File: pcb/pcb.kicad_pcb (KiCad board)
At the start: 2 copper layers, 70 x 21 mm, 20 parts, among them J1 BAT+, J2 BAT-, J3 Molex, SW1 Reset, SW2 Flash, U1 BOB-13263, U2 ESP-12F, U3 TP4056, U4 GY-521, U5 VREG

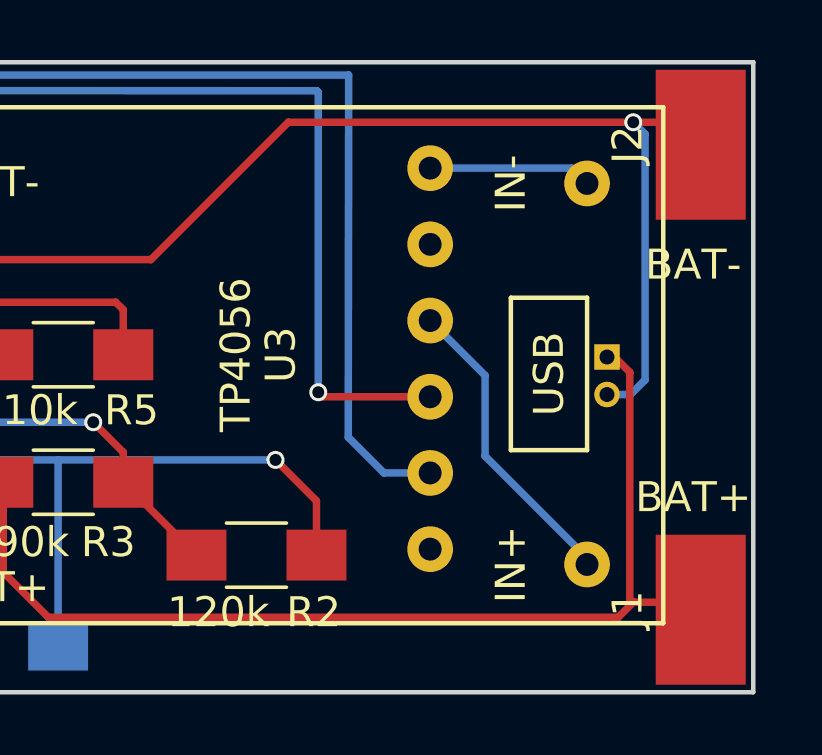
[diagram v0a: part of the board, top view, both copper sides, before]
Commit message: PCB: use a smaller FTDI breakout board
The CP2102 USB Micro breakout boards look like they fit between the
pins of the TP4056 breakout board, which simplifies installation.
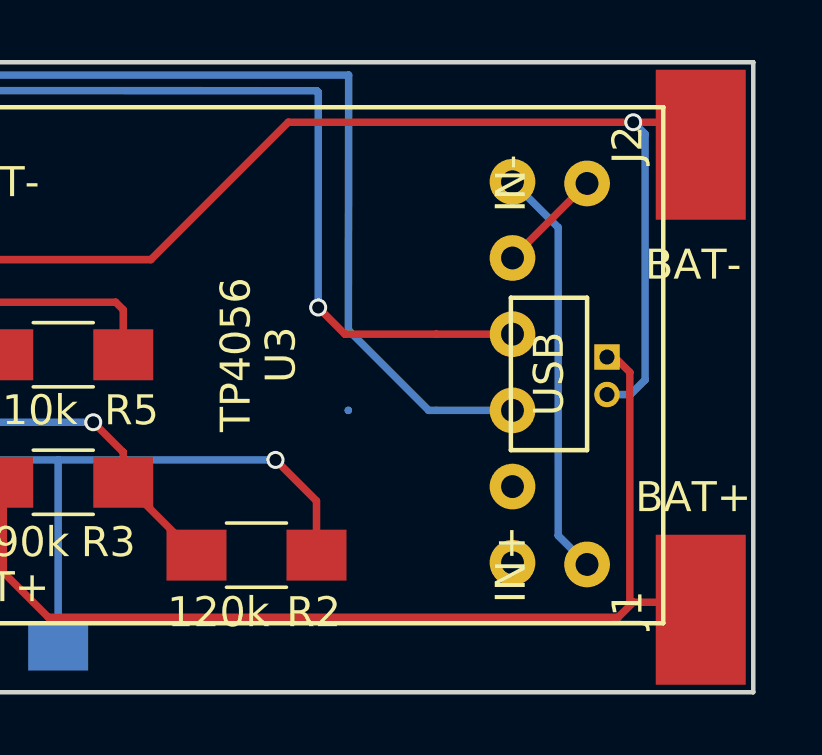
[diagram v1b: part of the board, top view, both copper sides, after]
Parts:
- U1: value BOB-13263 -> CP2102; footprint BOB13263:BOB-13263-TOP -> CP2102-BRK:CP2102-BREAKOUT
- moved U1 17.6 mm to (153.2, 105.7), turned to 0 degrees
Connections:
- U1 pad 2: /HostRX -> (no net)
- U1 pad 3: /HostTX -> /HostRX
- U1 pad 4: /USB+ -> /HostTX
- U1 pad 5: (no net) -> /USB-
- U1 pad 6: /USB- -> /USB+
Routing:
- net /USB+: track 10.3 -> 13.8 mm
- net /USB-: track 5.44 -> 3.51 mm

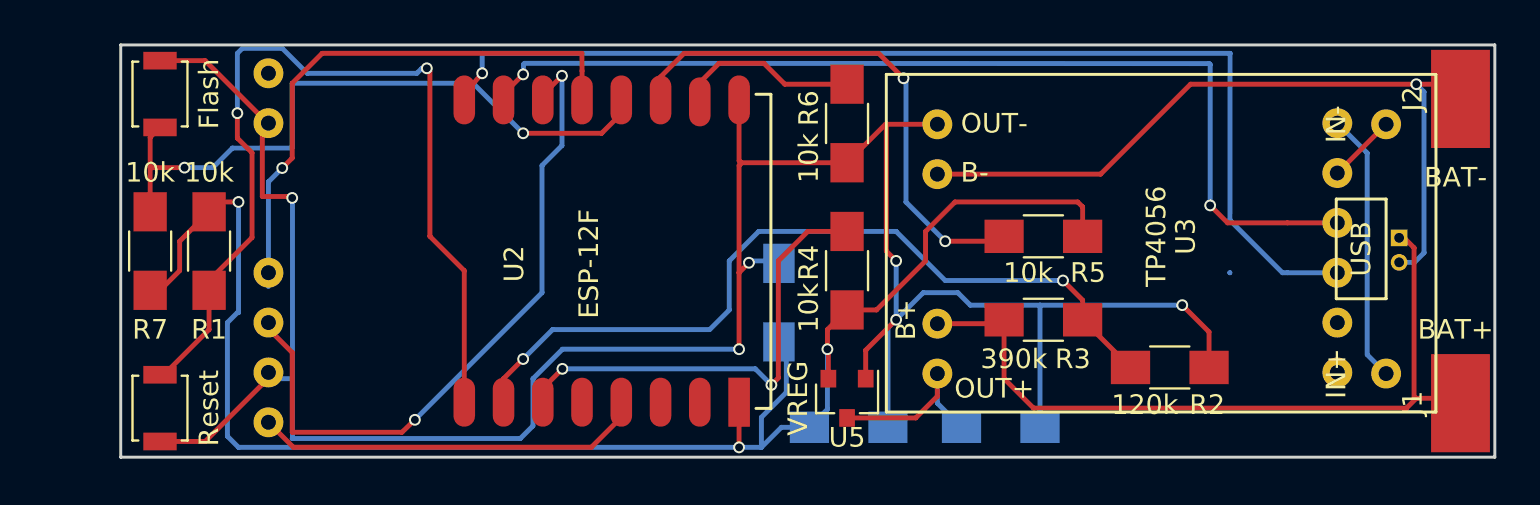
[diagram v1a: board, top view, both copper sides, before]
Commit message: Some more minor touch-ups
1. Remove silkscreen from pads which will take soldering
2. Fix some trace-via clearance issues (min 5 mil)
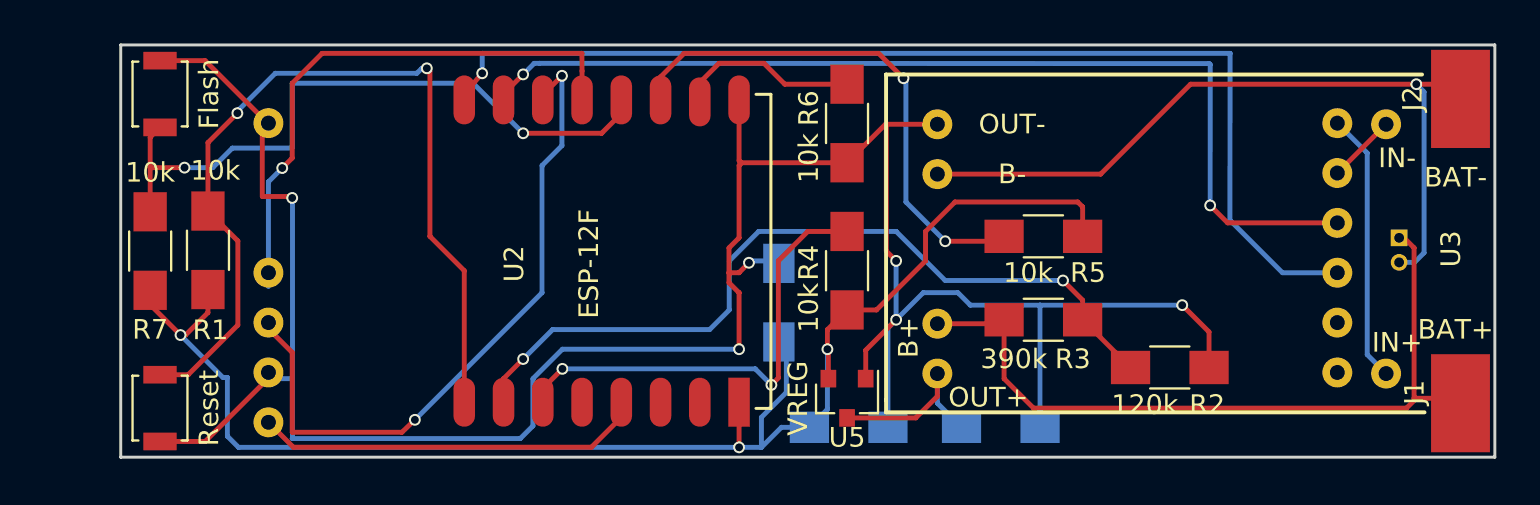
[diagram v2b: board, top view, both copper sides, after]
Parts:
- moved R1 0.07 mm to (114.7, 98.2), turned to 90 degrees
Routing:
- net /3.3+: track 84.7 -> 77.7 mm
- net Net-(R1-Pad2): track 46.2 -> 45.0 mm
- net /GND: track 129.2 -> 130.1 mm

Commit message: More trace cleanup:
1. Remove right angles
2. Thicker USB+/-, charger +/-, 3.3, GND traces
3. Improve 3.3 and GND routing: more like rails and traces to
components, less daisy-chaining
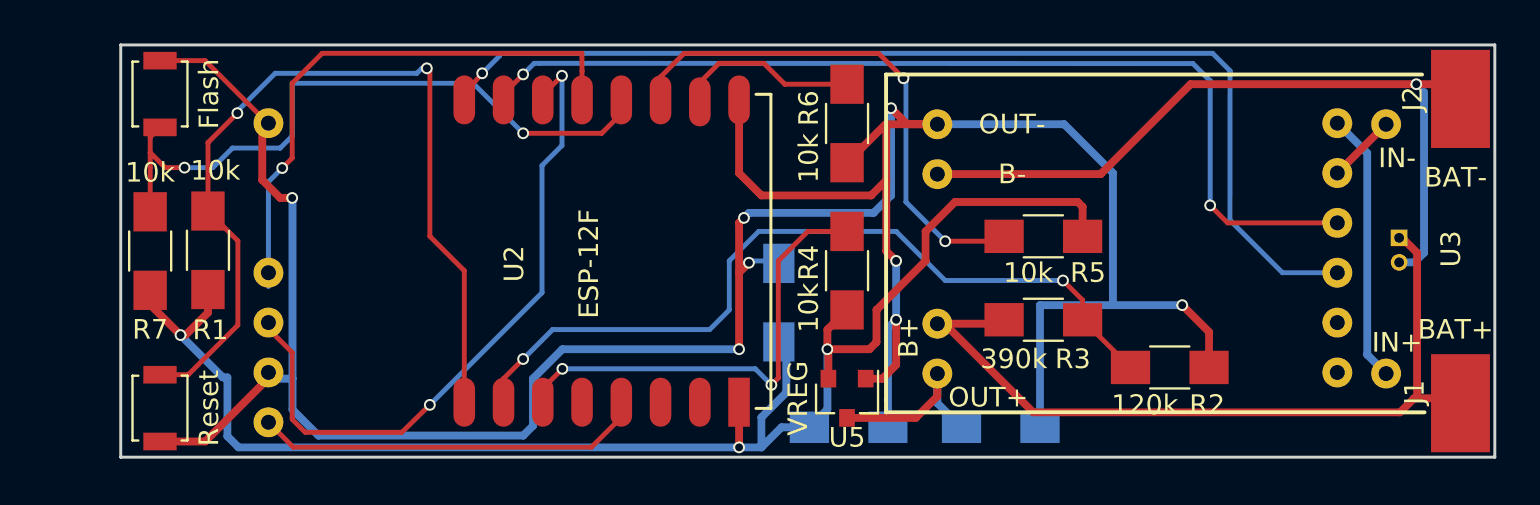
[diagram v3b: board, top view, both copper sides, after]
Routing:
- net /GND: track 130.1 -> 152.5 mm, vias 6 -> 8
- net /3.3+: track 77.7 -> 80.5 mm
- net /BAT+: track 39.6 -> 41.0 mm
- net /HostRX: track 56.6 -> 55.5 mm

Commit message: GY521 dimensions update (to match measured size on my workbench)
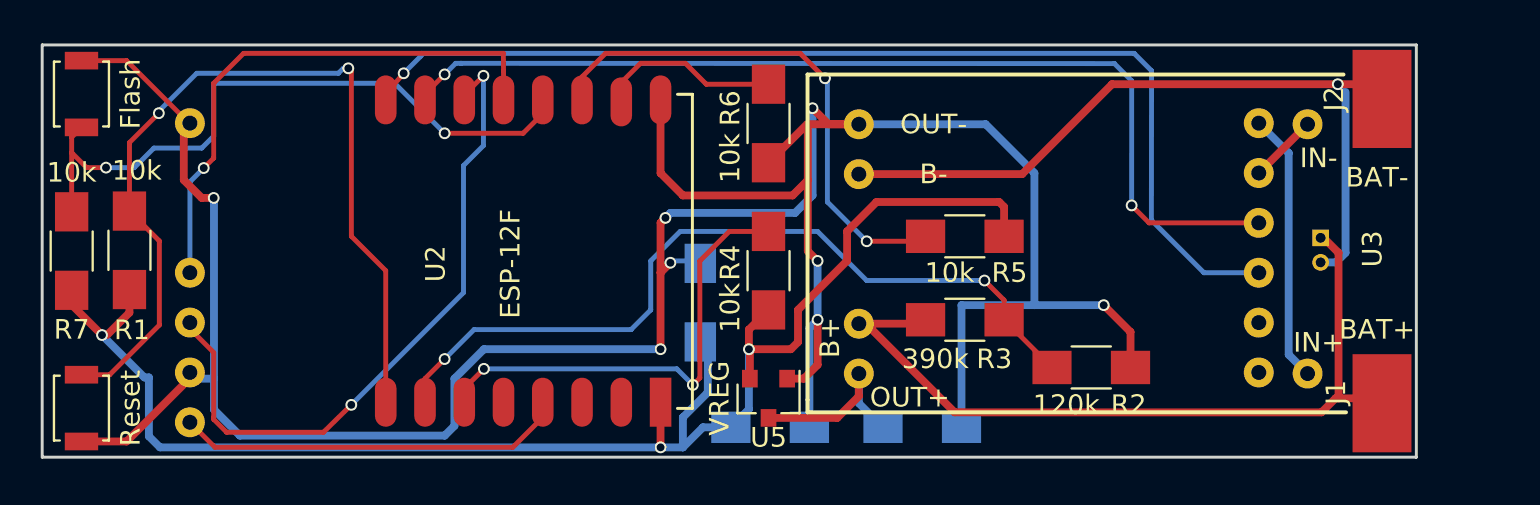
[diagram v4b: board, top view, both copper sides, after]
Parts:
- moved C1 4.00 mm to (139.8, 100.8)
- moved C2 4.00 mm to (151.1, 107.2)
- moved C3 4.00 mm to (143.3, 107.2)
- moved J1 4.00 mm to (174.5, 106.0)
- moved J2 4.00 mm to (174.5, 90.5)
- moved J3 4.00 mm to (171.4, 97.5)
- moved R1 4.00 mm to (110.7, 98.2)
- moved R2 4.00 mm to (159.7, 104.1)
- moved R3 4.00 mm to (153.2, 101.7)
- moved R4 4.00 mm to (143.2, 99.2)
- moved R5 4.00 mm to (153.2, 97.5)
- moved R6 4.00 mm to (143.2, 91.7)
- moved R7 4.00 mm to (107.7, 98.2)
- moved SW1 4.00 mm to (108.2, 106.2)
- moved SW2 4.00 mm to (108.2, 90.2)
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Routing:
- net /SDA: track 29.3 -> 28.6 mm

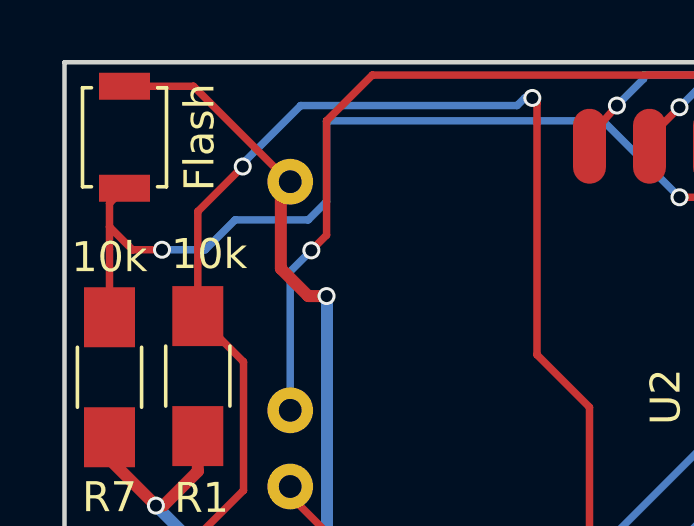
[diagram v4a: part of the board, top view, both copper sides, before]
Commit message: Move board in page (ugh)
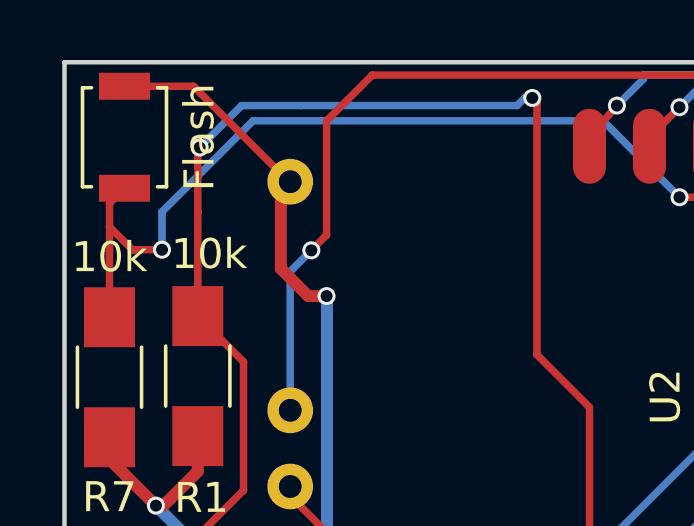
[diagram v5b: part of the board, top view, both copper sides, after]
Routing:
- net Net-(R1-Pad2): track 45.0 -> 46.2 mm
- net Net-(R7-Pad2): track 33.7 -> 32.8 mm
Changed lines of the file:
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@@
     (links 41)
     (no_connects 0)
-    (area 99.037601 87.234999 180.536601 118.560001)
+    (area 106.162599 87.634999 176.312601 108.785001)
     (thickness 1.6)
     (drawings 17)
@@
   (segment (start 151.2376 101.71) (end 151.0376 101.91) (width 0.25) (layer F.Cu) (net 5) (status 30))
   (segment (start 151.0376 101.91) (end 147.8376 101.91) (width 0.4) (layer F.Cu) (net 5) (status 30))
-  (segment (start 110.681 96.171) (end 110.681 92.6846) (width 0.25) (layer F.Cu) (net 6) (status 10))
-  (segment (start 112.1796 91.186) (end 112.1796 91.0844) (width 0.25) (layer B.Cu) (net 6))
+  (segment (start 110.681 92.71) (end 110.681 90.614) (width 0.25) (layer F.Cu) (net 6))
+  (segment (start 123.7376 99.21) (end 121.9876 97.46) (width 0.25) (layer F.Cu) (net 6))
+  (segment (start 121.9876 89.056) (end 121.9876 97.46) (width 0.25) (layer F.Cu) (net 6))
+  (segment (start 121.8316 88.9) (end 121.9876 89.056) (width 0.25) (layer F.Cu) (net 6))
+  (segment (start 123.7376 99.21) (end 123.7376 105.21) (width 0.25) (layer F.Cu) (net 6) (status 20))
+  (via (at 121.8316 88.9) (size 0.6) (drill 0.4) (layers F.Cu B.Cu) (net 6))
+  (segment (start 121.5776 88.9) (end 121.8316 88.9) (width 0.25) (layer B.Cu) (net 6))
+  (segment (start 121.3236 89.154) (end 121.5776 88.9) (width 0.25) (layer B.Cu) (net 6))
   (segment (start 114.11 89.154) (end 121.3236 89.154) (width 0.25) (layer B.Cu) (net 6))
-  (segment (start 112.1796 91.0844) (end 114.11 89.154) (width 0.25) (layer B.Cu) (net 6))
-  (segment (start 121.3236 89.154) (end 121.5776 88.9) (width 0.25) (layer B.Cu) (net 6))
-  (segment (start 121.5776 88.9) (end 121.8316 88.9) (width 0.25) (layer B.Cu) (net 6))
-  (via (at 121.8316 88.9) (size 0.6) (drill 0.4) (layers F.Cu B.Cu) (net 6))
-  (via (at 112.1796 91.186) (size 0.6) (drill 0.4) (layers F.Cu B.Cu) (net 6))
-  (segment (start 123.7376 99.21) (end 123.7376 105.21) (width 0.25) (layer F.Cu) (net 6) (status 20))
-  (segment (start 121.8316 88.9) (end 121.9876 89.056) (width 0.25) (layer F.Cu) (net 6))
-  (segment (start 121.9876 89.056) (end 121.9876 97.46) (width 0.25) (layer F.Cu) (net 6))
-  (segment (start 123.7376 99.21) (end 121.9876 97.46) (width 0.25) (layer F.Cu) (net 6))
-  (segment (start 110.681 92.6846) (end 112.1796 91.186) (width 0.25) (layer F.Cu) (net 6))
+  (segment (start 112.141 89.154) (end 114.11 89.154) (width 0.25) (layer B.Cu) (net 6))
+  (segment (start 110.744 90.551) (end 112.141 89.154) (width 0.25) (layer B.Cu) (net 6))
+  (via (at 110.744 90.551) (size 0.6) (drill 0.4) (layers F.Cu B.Cu) (net 6))
+  (segment (start 110.681 90.614) (end 110.744 90.551) (width 0.25) (layer F.Cu) (net 6))
+  (segment (start 110.681 96.171) (end 110.681 92.71) (width 0.25) (layer F.Cu) (net 6) (status 10))
+  (segment (start 110.681 92.71) (end 110.681 92.6846) (width 0.25) (layer F.Cu) (net 6) (status 10))
   (segment (start 108.2376 104.51) (end 109.676 104.51) (width 0.25) (layer F.Cu) (net 6) (status 10))
   (segment (start 112.205 97.695) (end 110.681 96.171) (width 0.25) (layer F.Cu) (net 6) (status 20))
@@
   (via (at 139.383 105.029) (size 0.6) (drill 0.4) (layers F.Cu B.Cu) (net 17))
   (segment (start 139.7376 104.6744) (end 139.383 105.029) (width 0.25) (layer F.Cu) (net 17))
+  (segment (start 109.4876 93.96) (end 109.4876 92.6964) (width 0.25) (layer B.Cu) (net 18))
+  (segment (start 126.7376 92.21) (end 130.7376 92.21) (width 0.25) (layer F.Cu) (net 18))
+  (segment (start 109.4876 93.96) (end 108.522 93.96) (width 0.25) (layer F.Cu) (net 18))
+  (via (at 109.4876 93.96) (size 0.6) (drill 0.4) (layers F.Cu B.Cu) (net 18))
+  (segment (start 114.9736 89.662) (end 124.1896 89.662) (width 0.25) (layer B.Cu) (net 18))
+  (segment (start 131.7376 91.21) (end 130.7376 92.21) (width 0.25) (layer F.Cu) (net 18) (status 10))
+  (segment (start 124.1896 89.662) (end 126.7376 92.21) (width 0.25) (layer B.Cu) (net 18))
+  (via (at 126.7376 92.21) (size 0.6) (drill 0.4) (layers F.Cu B.Cu) (net 18))
+  (segment (start 108.502 93.96) (end 107.7376 93.1956) (width 0.25) (layer F.Cu) (net 18))
   (segment (start 108.522 93.96) (end 108.502 93.96) (width 0.25) (layer F.Cu) (net 18))
-  (segment (start 108.502 93.96) (end 107.7376 93.1956) (width 0.25) (layer F.Cu) (net 18))
-  (segment (start 114.364 92.964) (end 114.9736 92.3544) (width 0.25) (layer B.Cu) (net 18))
-  (segment (start 114.9736 92.3544) (end 114.9736 89.662) (width 0.25) (layer B.Cu) (net 18))
-  (via (at 126.7376 92.21) (size 0.6) (drill 0.4) (layers F.Cu B.Cu) (net 18))
-  (segment (start 124.1896 89.662) (end 126.7376 92.21) (width 0.25) (layer B.Cu) (net 18))
-  (segment (start 131.7376 91.21) (end 130.7376 92.21) (width 0.25) (layer F.Cu) (net 18) (status 10))
-  (segment (start 114.9736 89.662) (end 124.1896 89.662) (width 0.25) (layer B.Cu) (net 18))
-  (segment (start 110.9296 93.96) (end 111.9256 92.964) (width 0.25) (layer B.Cu) (net 18))
-  (segment (start 111.9256 92.964) (end 114.364 92.964) (width 0.25) (layer B.Cu) (net 18))
-  (via (at 109.4876 93.96) (size 0.6) (drill 0.4) (layers F.Cu B.Cu) (net 18))
-  (segment (start 109.4876 93.96) (end 108.522 93.96) (width 0.25) (layer F.Cu) (net 18))
-  (segment (start 109.4876 93.96) (end 110.9296 93.96) (width 0.25) (layer B.Cu) (net 18))
-  (segment (start 126.7376 92.21) (end 130.7376 92.21) (width 0.25) (layer F.Cu) (net 18))
+  (segment (start 112.522 89.662) (end 114.9736 89.662) (width 0.25) (layer B.Cu) (net 18))
+  (segment (start 109.4876 92.6964) (end 112.522 89.662) (width 0.25) (layer B.Cu) (net 18))
   (segment (start 107.7376 96.21) (end 107.7376 93.96) (width 0.25) (layer F.Cu) (net 18) (status 10))
   (segment (start 107.7376 93.96) (end 107.7376 93.1956) (width 0.25) (layer F.Cu) (net 18))
